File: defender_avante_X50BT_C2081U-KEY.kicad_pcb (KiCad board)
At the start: 2 copper layers, 172.7 x 61 mm, 86 parts, among them CN301 CONNECTOR_M_006_20_SPECIAL, J300 JUMPER, J301 JUMPER, J302 JUMPER, J303 JUMPER, J304 JUMPER, J305 JUMPER, J306 JUMPER, J307 JUMPER, J308 JUMPER, J309 JUMPER, J310 JUMPER, J311 JUMPER, J312 JUMPER, J313 JUMPER, J314 JUMPER, J315 JUMPER, J316 JUMPER, J317 JUMPER, J318 JUMPER, J319 JUMPER, J320 JUMPER, J321 JUMPER, J322 JUMPER, J323 JUMPER, J324 JUMPER, J325 JUMPER, J326 JUMPER, J327 JUMPER, J328 JUMPER, J329 JUMPER, J330 JUMPER, J331 JUMPER, J332 JUMPER, J333 JUMPER, J334 JUMPER, J335 JUMPER, J336 JUMPER, Q300 BJT_NPN_GENERAL, U300 TM1668

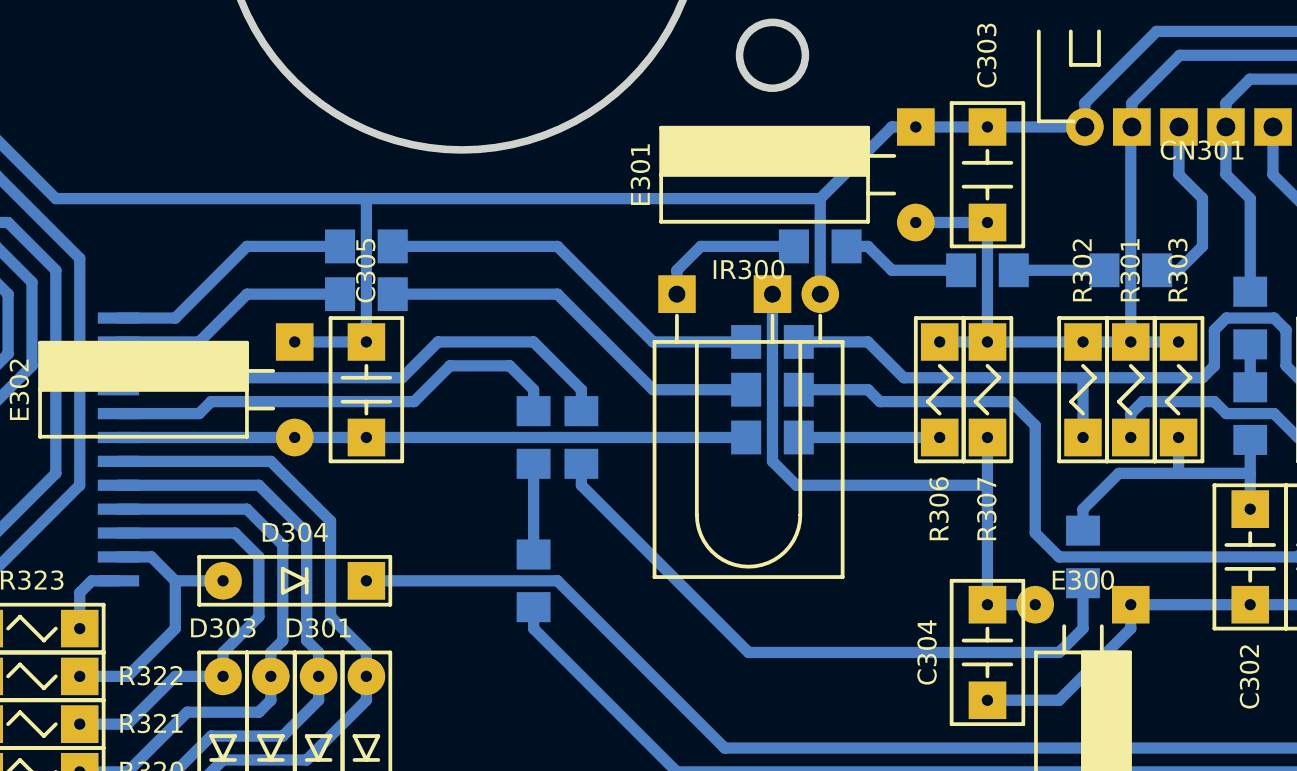
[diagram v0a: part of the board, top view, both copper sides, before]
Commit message: Ширина шины питания увеличена с 0.6 до 1.5 мм
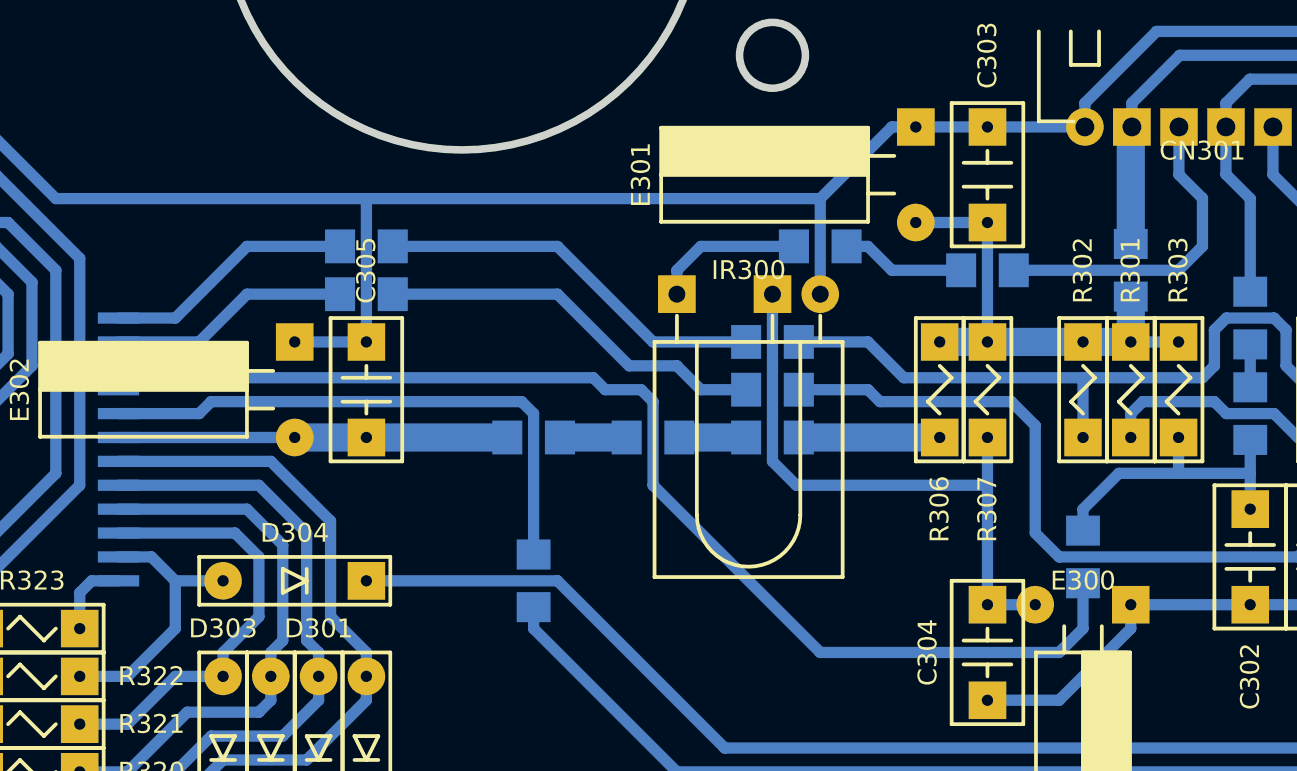
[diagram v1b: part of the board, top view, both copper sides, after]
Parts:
- moved J309 3.81 mm to (162.6, 99.1), turned to 0 degrees
- turned J302 to 90 degrees
- turned J310 to 0 degrees
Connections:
- J302 pad J: /IR -> V
- J309 pad J: /STB -> /IC_+5V
- J310 pad J: /K2 -> /IC_+5V
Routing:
- net /IC_+5V: track 40.9 -> 35.3 mm
- net /IR: track 29.3 -> 32.1 mm
- net V: track 72.5 -> 69.7 mm
- net /STB: track 104.0 -> 104.9 mm

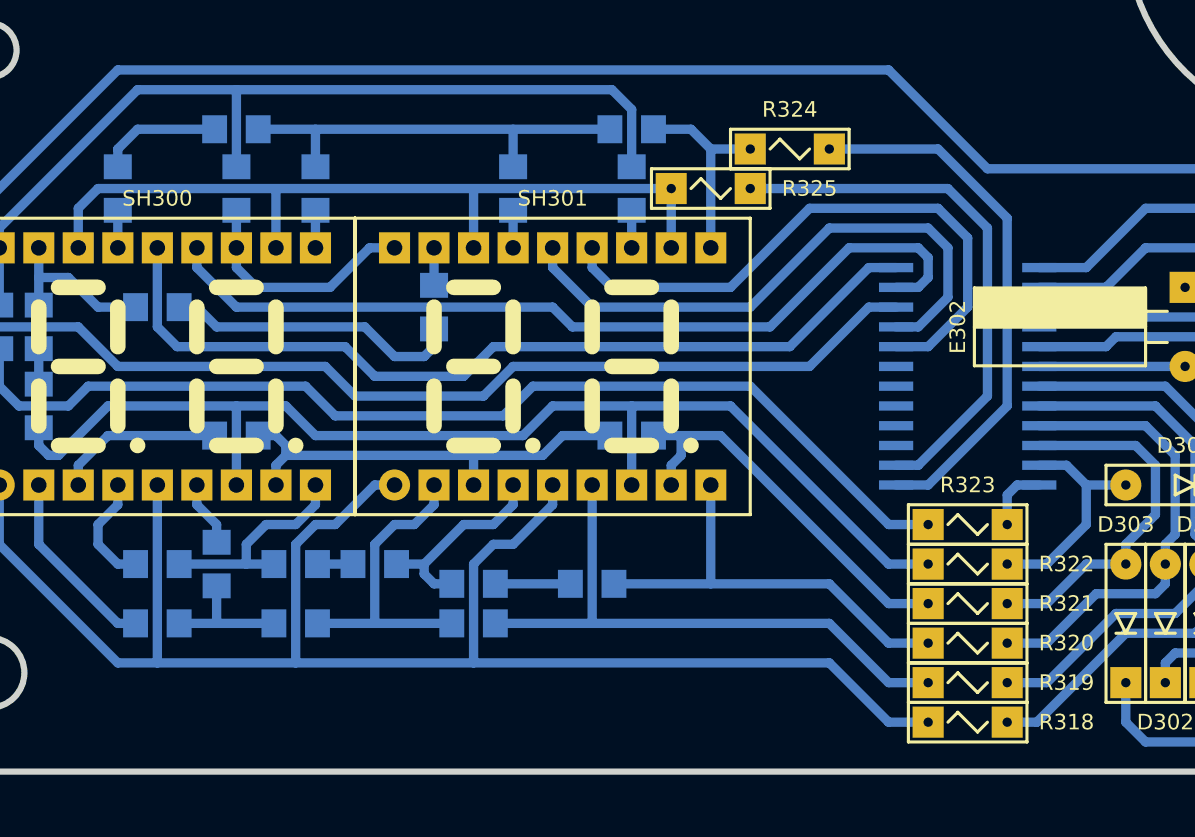
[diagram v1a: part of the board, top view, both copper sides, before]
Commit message: Удалены резисторы R318…R325
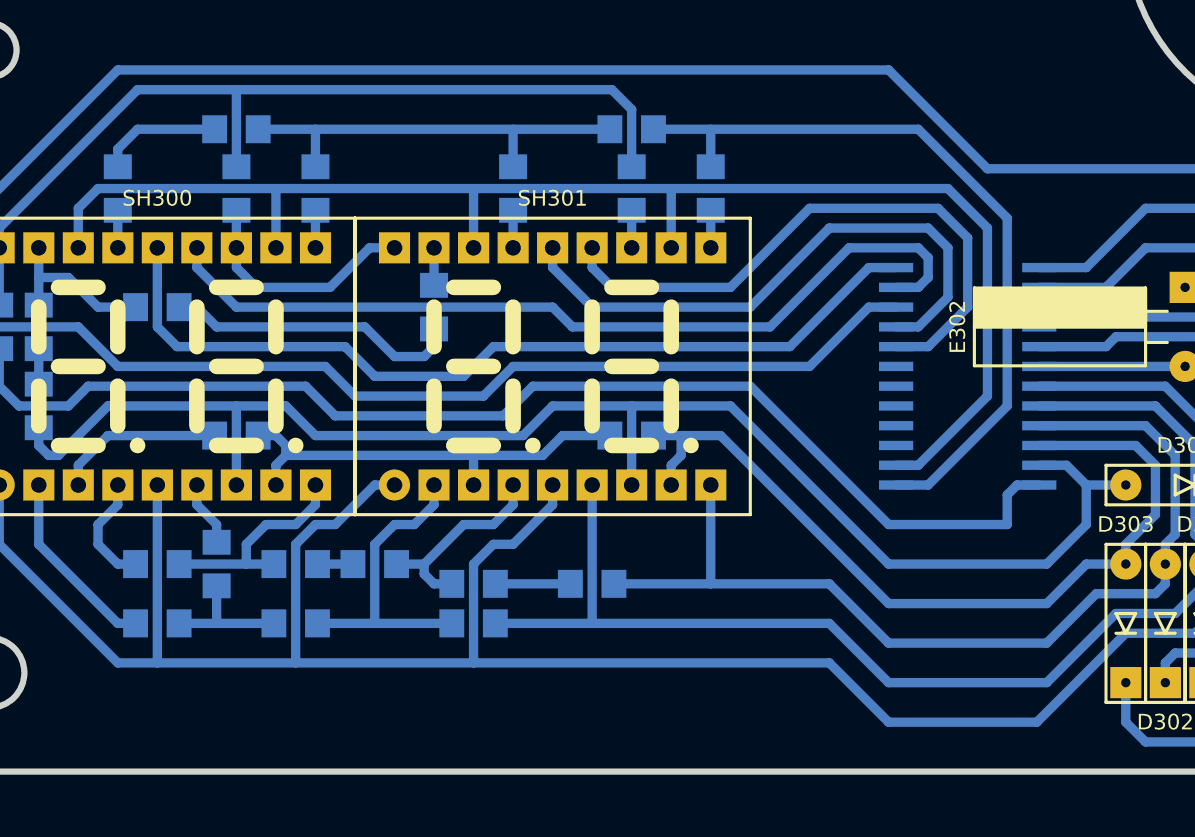
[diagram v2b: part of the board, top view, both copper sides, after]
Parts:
- removed R318, R319, R320, R321, R322, R323, R324, R325: RESISTOR_GENERAL, KCL:R-MFR-12
- added J314: JUMPER, KCL:J-SMD-1206, B.Cu at (113.0, 87.6)
- renumbered J314 to J315, J315 to J316, J316 to J317, J317 to J318, J318 to J319, J319 to J320, J320 to J321, J321 to J322, J322 to J323, J323 to J324, J324 to J325, J325 to J326, J326 to J327, J327 to J328, J328 to J329, J329 to J330, J330 to J331, J331 to J332, J332 to J333, J333 to J334, J334 to J335, J335 to J336, J336 to J337
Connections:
- D300 pad A: /KS1 -> /E
- D301 pad A: /KS2 -> /D
- D302 pad A: /KS3 -> /DP
- D303 pad A: /KS4 -> /C
- D304 pad A: /KS5 -> /G
- U300 pad 10: /KS4 -> /C
- U300 pad 11: /KS5 -> /G
- U300 pad 12: Net-(R323-Pad2) -> /F
- U300 pad 13: Net-(R324-Pad1) -> /B
- U300 pad 14: Net-(R325-Pad1) -> /A
- U300 pad 15: (no net) -> Net-(U300-Pad15)
- U300 pad 16: (no net) -> Net-(U300-Pad16)
- U300 pad 17: (no net) -> Net-(U300-Pad17)
- U300 pad 18: (no net) -> Net-(U300-Pad18)
- U300 pad 19: (no net) -> Net-(U300-Pad19)
- U300 pad 4: (no net) -> Net-(U300-Pad4)
- U300 pad 7: /KS1 -> /E
- U300 pad 8: /KS2 -> /D
- U300 pad 9: /KS3 -> /DP
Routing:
- net /E: track 109.5 -> 156.4 mm
- net /KS1: track 41.8 -> 0.00 mm
- net /D: track 83.0 -> 123.6 mm
- net /A: track 52.6 -> 92.5 mm
- net /B: track 55.6 -> 93.8 mm
- net /KS2: track 35.5 -> 0.00 mm
- net /DP: track 69.6 -> 104.5 mm
- net Net-(R325-Pad1): track 34.8 -> 0.00 mm
- net Net-(R324-Pad1): track 34.6 -> 0.00 mm
- net /KS3: track 29.8 -> 0.00 mm
- net /C: track 64.5 -> 93.4 mm
- net /KS4: track 23.8 -> 0.00 mm
- net /G: track 110.3 -> 130.1 mm
- net /KS5: track 14.8 -> 0.00 mm
- net /F: track 144.7 -> 154.0 mm
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
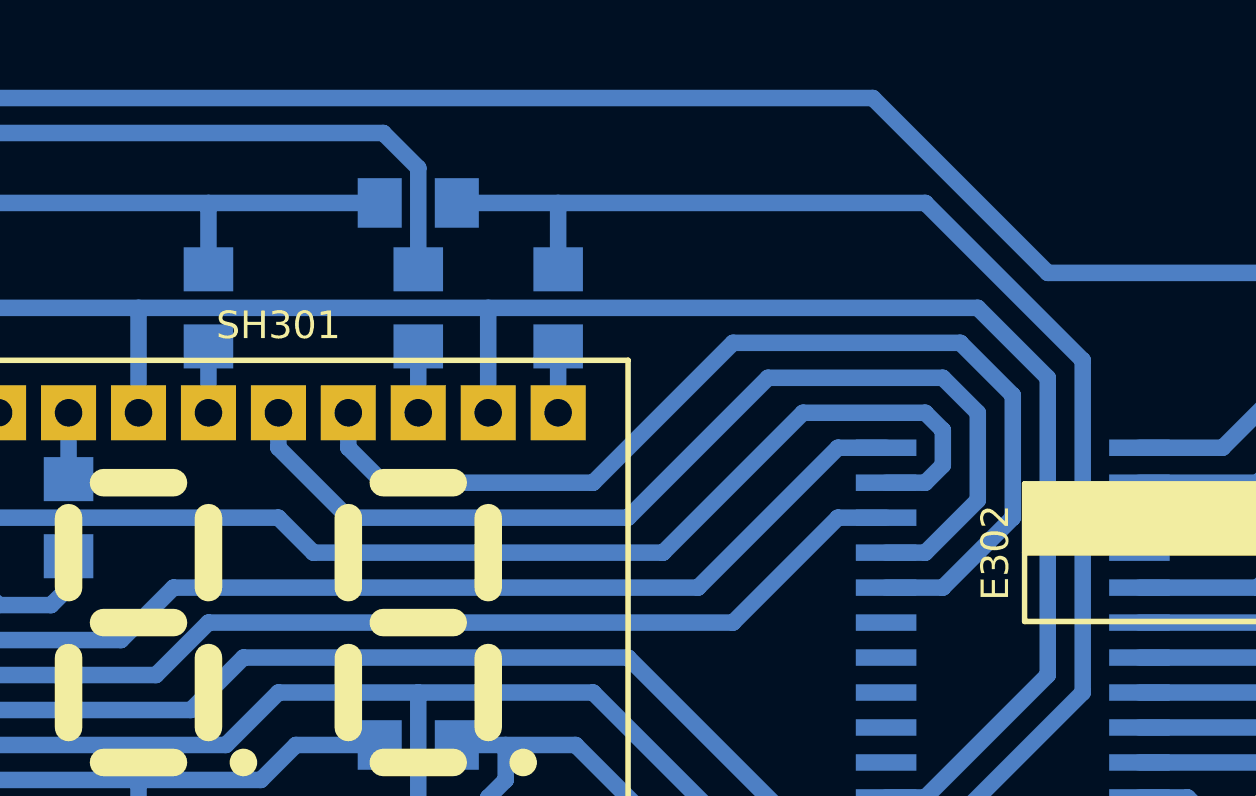
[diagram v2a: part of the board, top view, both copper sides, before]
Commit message: Добавлена выводная перемычка J338
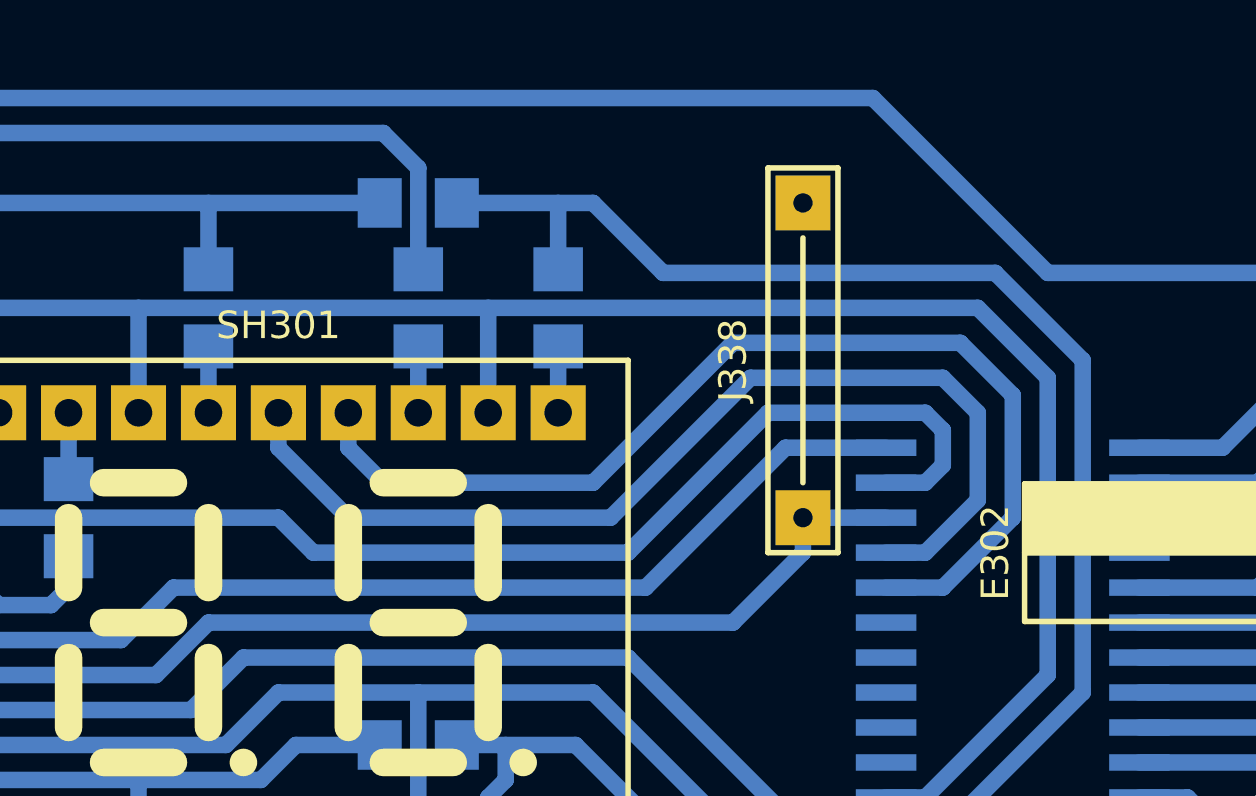
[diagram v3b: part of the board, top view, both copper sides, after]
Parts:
- added J338: JUMPER, KCL:J-THT-d0.6-P11.43, F.Cu at (121.9, 89.5)
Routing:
- net COM: track 321.7 -> 322.4 mm

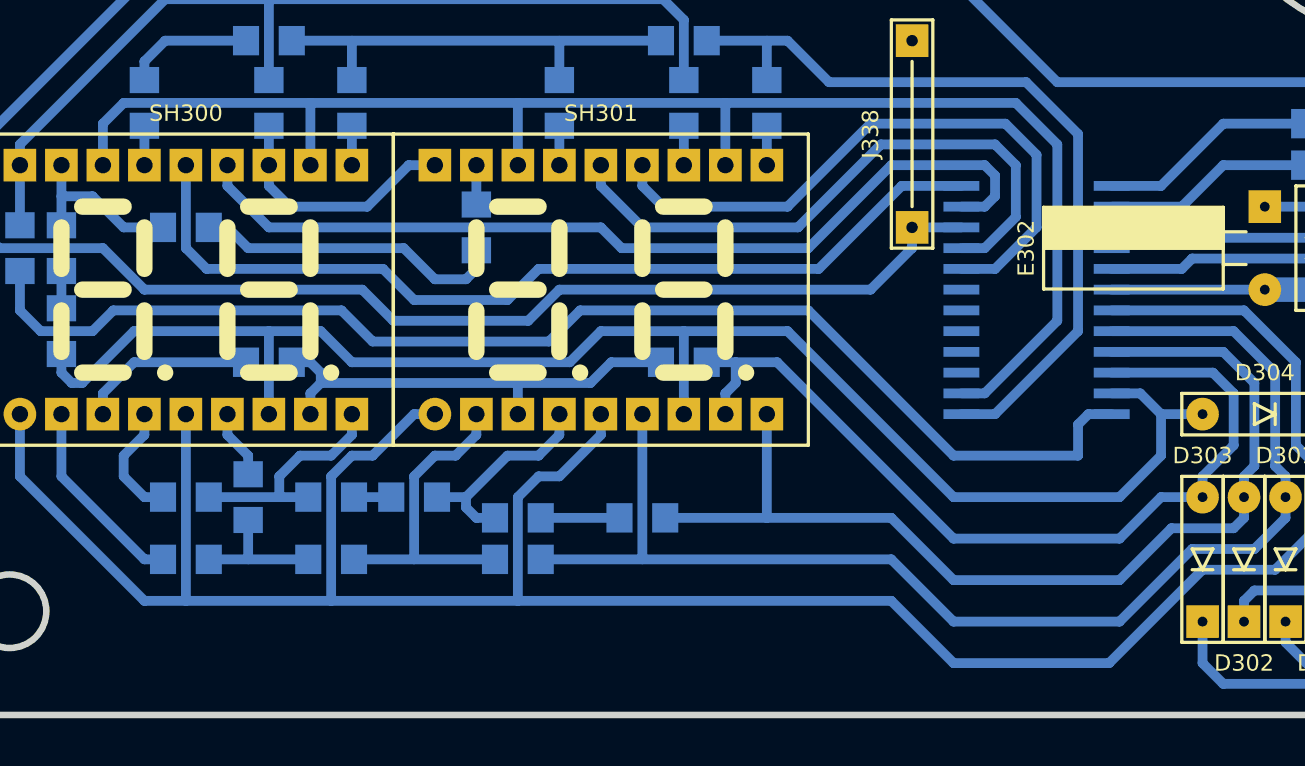
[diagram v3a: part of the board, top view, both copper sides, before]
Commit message: Положение дорожек скорректировано в связи с удалением резисторов. Удалены верхние слои КП J338
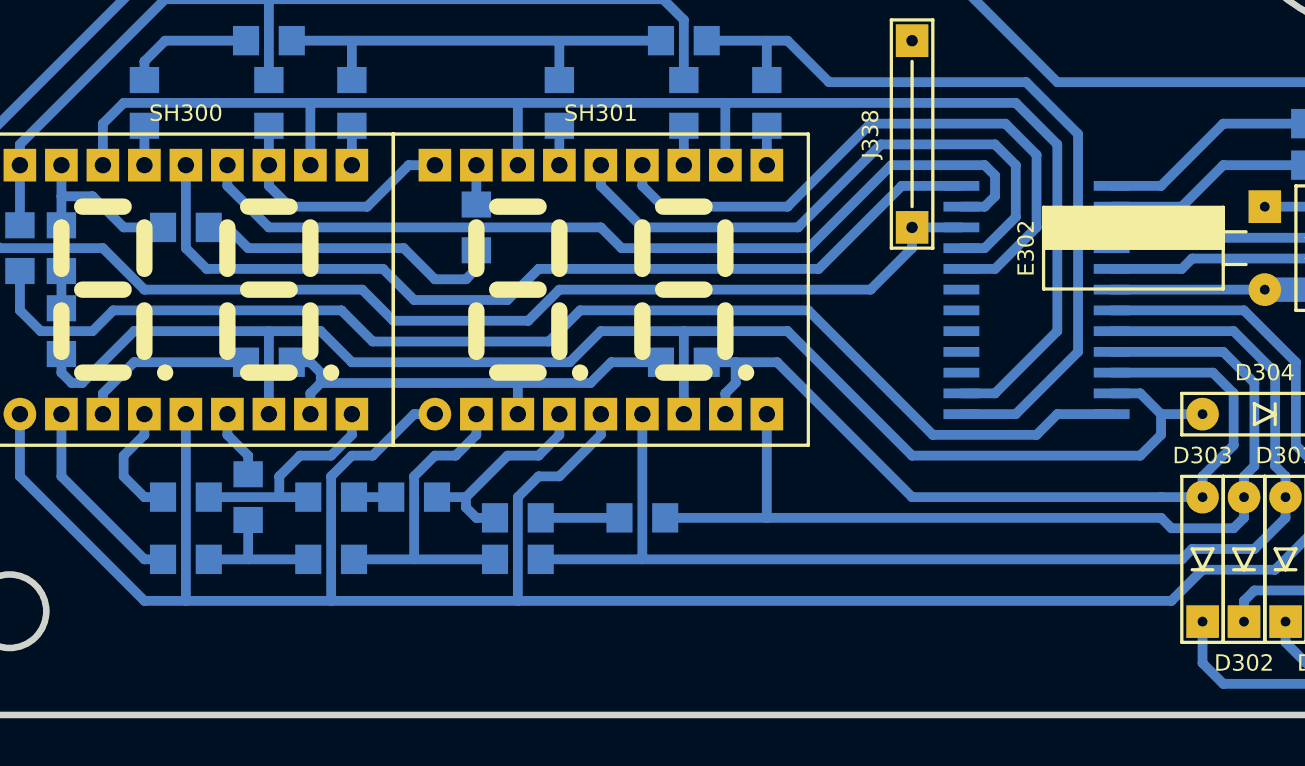
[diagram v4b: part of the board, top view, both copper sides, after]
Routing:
- net /E: track 156.4 -> 153.2 mm
- net /D: track 123.6 -> 120.4 mm
- net /G: track 130.1 -> 127.3 mm
- net /DP: track 104.5 -> 101.9 mm
- net /F: track 154.0 -> 151.8 mm
- net /C: track 93.4 -> 91.3 mm
- net /B: track 93.8 -> 94.5 mm
